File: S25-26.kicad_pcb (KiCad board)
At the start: 6 copper layers, 90 x 90 mm, 139 parts, among them IC1 CMV4000-3E5M0PN, IC10 DS90LV048ATM_NOPB, IC2 MXL86110I-AQB-R, IC3 NCV317BD2TR4G, IC4 MT29F2G01ABAGDWB-IT_G_TR, IC5 MT29F2G01ABAGDWB-IT_G_TR, IC6 XMC7200D-E272K8384AA, IC7 DS90LV011AHMF_NOPB, IC8 DS90LV048ATM_NOPB, IC9 DS90LV048ATM_NOPB, J1 DC_IN_PADS, J2 Conn_01x04_Pin, J3 Conn_01x02_Pin, J4 RJ45_RB1-125B8G1A, Q1 ZXT849K, U1 TPS73601MDRBREP, U2 TPS73601MDRBREP, Y1 DSC1101DM2-012.0000

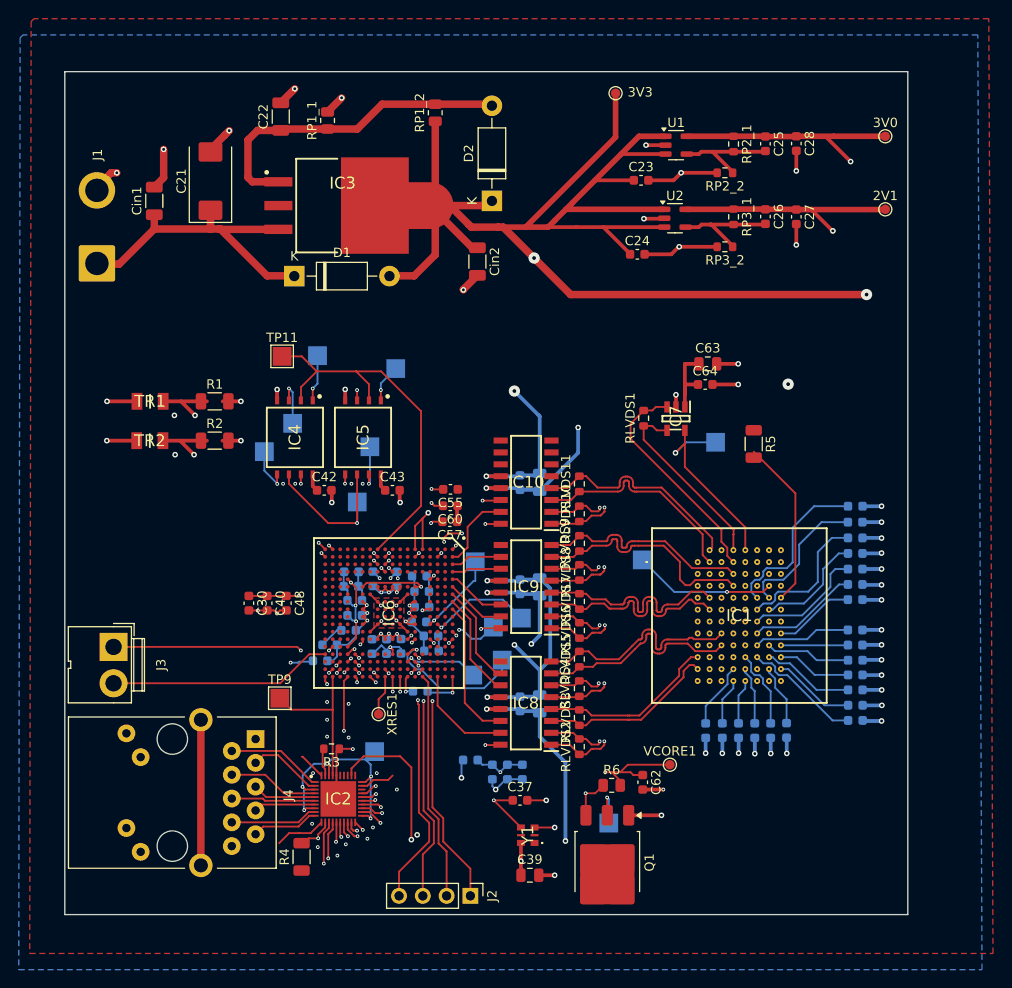
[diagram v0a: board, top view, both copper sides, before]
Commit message: Watch Out: David's Mounting Holes
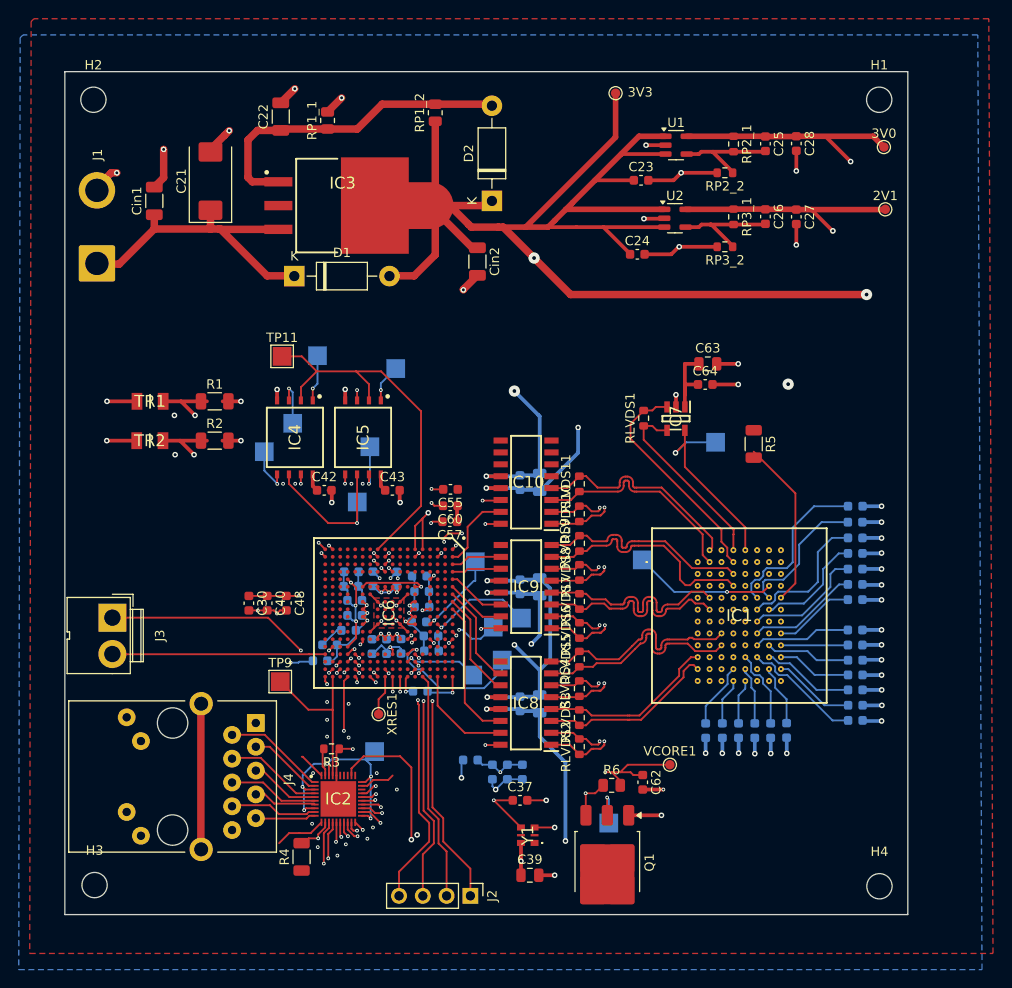
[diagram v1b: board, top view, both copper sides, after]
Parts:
- added H1: MountingHole, MountingHole:MountingHole_2.7mm, F.Cu at (195.3, 53.2)
- added H2: MountingHole, MountingHole:MountingHole_2.7mm, F.Cu at (111.5, 53.2)
- added H3: MountingHole, MountingHole:MountingHole_2.7mm, F.Cu at (111.6, 137.1)
- added H4: MountingHole, MountingHole:MountingHole_2.7mm, F.Cu at (195.4, 137.2)
- moved J3 3.12 mm to (113.5, 108.5)
- moved TP9 1.78 mm to (131.4, 115.3)
- moved J4 1.72 mm to (128.8, 119.7)
- moved 3V0 1.16 mm to (195.8, 58.2)
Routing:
- net /SCB3_RX: track 23.6 -> 25.4 mm
- net /PHY_LED0: track 58.7 -> 60.4 mm
- net /BI_DD_N: track 7.15 -> 5.64 mm
- net /ETH0_REF_CLK: track 16.8 -> 17.6 mm
- net /BI_DB_P: track 9.70 -> 10.5 mm
- net /BI_DA_P: track 10.3 -> 11.0 mm
- net /BI_DB_N: track 6.79 -> 7.54 mm
- net /BI_DC_P: track 8.97 -> 9.72 mm
- net /SCB3_TX: track 23.9 -> 23.2 mm

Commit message: Lots of small changes
Some power and ground planes need to be looked at
All parts need to be reexamined before ordering
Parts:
- removed C21: 10uF, Capacitor_Tantalum_SMD:CP_EIA-7343-31_Kemet-D
- removed C22: 10uF, Capacitor_SMD:C_1206_3216Metric
- removed Cin1, Cin2: 1uF, Capacitor_SMD:C_1206_3216Metric
- removed D2: 1N4002, Diode_THT:D_DO-41_SOD81_P10.16mm_Horizontal
- removed RP1_1: 165, Resistor_SMD:R_0805_2012Metric
- removed RP1_2: 100, Resistor_SMD:R_0805_2012Metric
- added C71: 100uF, Capacitor_SMD:C_1206_3216Metric, F.Cu at (142.9, 64.5)
- added C72: 10nF, Capacitor_SMD:C_1206_3216Metric, F.Cu at (129.0, 71.3)
- added C73: 150pF, Capacitor_SMD:C_1206_3216Metric, F.Cu at (131.4, 59.5)
- added C74: 0.1uF, Capacitor_SMD:C_1206_3216Metric, F.Cu at (135.1, 59.5)
- added C75: 1500pF, Capacitor_SMD:C_1206_3216Metric, F.Cu at (135.2, 64.5)
- added C76: 4.7uF, Capacitor_SMD:C_1206_3216Metric, F.Cu at (116.2, 63.9)
- added C77: 4.7uF, Capacitor_SMD:C_1206_3216Metric, F.Cu at (120.0, 64.0)
- added J5: Conn_01x04_Pin, Connector_PinHeader_2.54mm:PinHeader_1x04_P2.54mm_Vertical, F.Cu at (110.3, 85.4)
- added L1: SRP6060FA-150M, SamacSys_Parts:SRP6060FA150M, F.Cu at (135.2, 70.9)
- added R10: 247k, Resistor_SMD:R_1206_3216Metric, F.Cu at (121.7, 54.0)
- added R11: 33k, Resistor_SMD:R_1206_3216Metric, F.Cu at (127.1, 54.0)
- added R7: 10k, Resistor_SMD:R_1206_3216Metric, F.Cu at (139.1, 64.5)
- added R8: 5.9k, Resistor_SMD:R_1206_3216Metric, F.Cu at (139.0, 59.5)
- added R9: 549, Resistor_SMD:R_1206_3216Metric, F.Cu at (135.1, 54.5)
- D1: value 1N4002 -> MBRS340T3G; footprint Diode_THT:D_DO-41_SOD81_P10.16mm_Horizontal -> SamacSys_Parts:DIOM8059X261N
- IC3: value NCV317BD2TR4G -> TPS5430DDAR; footprint SamacSys_Parts:TO254P1420X457-4N -> SamacSys_Parts:SOIC127P600X170-9N
- J2: value Conn_01x04_Pin -> Conn_01x06_Pin; footprint Connector_PinHeader_2.54mm:PinHeader_1x04_P2.54mm_Vertical -> Connector_PinHeader_2.54mm:PinHeader_1x06_P2.54mm_Vertical
- J3: value Conn_01x02_Pin -> Conn_01x04_Pin; footprint Connector:JWT_A3963_1x02_P3.96mm_Vertical -> Connector_PinHeader_2.54mm:PinHeader_1x04_P2.54mm_Vertical
- J4: value RJ45_RB1-125B8G1A -> RJ45_JXD1-0001NL
- U1, U2: value TPS73601MDRBREP -> TPS73601MDBVREP
- moved J4 17.0 mm to (117.2, 132.2)
- moved IC3 11.2 mm to (126.2, 64.8), turned to 180 degrees
- moved D1 10.9 mm to (122.0, 73.0), turned to 180 degrees
- moved J3 6.18 mm to (110.2, 103.3), turned to 0 degrees
- moved J1 5.28 mm to (111.8, 65.4), turned to -90 degrees
- moved R6 0.28 mm to (166.5, 126.3), turned to 180 degrees
- moved U2 0.13 mm to (173.7, 65.9)
- moved RLVDS1 0.13 mm to (170.3, 87.3)
- moved RLVDS5 0.11 mm to (163.4, 113.0)
- moved RLVDS4 0.10 mm to (163.4, 116.2)
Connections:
- net /JTAG_SWCLK renamed /Processing/SWJ_SWCLK_TCLK
- net /JTAG_SWDIO renamed /Processing/SWJ_SWDIO_TMS
- net /JTAG_SWO renamed /Processing/SWJ_SWO_TDO
- net /JTAG_TDI renamed /Processing/SWJ_SWDOE_TDI
- net /SCB3_RX renamed /Processing/SCB3_RX (P17.1)
- D1 pad 1: /Voltage Regulation/DC_LINE_IN_28V -> Net-(D1-K)
- D1 pad 2: +3V3 -> GND
- IC3 pad 3: /Voltage Regulation/DC_LINE_IN_28V -> unconnected-(IC3-NC_2-Pad3)
- IC3 pad 4: +3V3 -> Net-(IC3-VSENSE)
- IC6 pad A14: unconnected-(IC6B-P2.0-PadA14) -> /Processing/SWJ_TRSTN
- IC6 pad R1: unconnected-(IC6B-P12.0-PadR1) -> /Processing/SCB8_RX
- IC6 pad R2: unconnected-(IC6B-P12.1-PadR2) -> /Processing/SCB8_TX
- IC6 pad R3: unconnected-(IC6B-P12.2-PadR3) -> /Processing/SCB8_RTS
- IC6 pad T1: unconnected-(IC6B-P12.3-PadT1) -> /Processing/SCB8_CTS
- IC6 pad T15: unconnected-(IC6B-P17.4-PadT15) -> /Processing/SCB3_CTS
- IC6 pad U15: unconnected-(IC6B-P17.3-PadU15) -> /Processing/SCB3_RTS
- IC6 pad V15: /SCB3_TX -> /Processing/SCB3_TX (P17.2)
- J3 pad 2: /SCB3_TX -> /Processing/SCB3_CTS
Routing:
- net +3V3: track 543.4 -> 482.0 mm
- net /Processing/SCB8_RX: track 0.00 -> 35.8 mm
- net /Processing/SCB8_TX: track 0.00 -> 33.6 mm, vias 0 -> 2
- net /Processing/SCB8_CTS: track 0.00 -> 33.0 mm
- net /Processing/SCB8_RTS: track 0.00 -> 32.9 mm, vias 0 -> 2
- net GND: track 549.8 -> 517.8 mm, vias 95 -> 90
- net Net-(IC3-BOOT): track 35.1 -> 3.16 mm
- net /Processing/SCB3_CTS: track 0.00 -> 31.8 mm, vias 0 -> 2
- net /Processing/SWJ_TRSTN: track 0.00 -> 31.5 mm, vias 0 -> 2
- net /Processing/SCB3_RTS: track 0.00 -> 28.1 mm, vias 0 -> 2
- net /Processing/SCB3_TX (P17.2): track 0.00 -> 27.7 mm
- net /SCB3_TX: track 23.2 -> 0.00 mm
- net /PHY_LED0: track 60.4 -> 42.1 mm
- net Net-(D1-K): track 0.00 -> 16.9 mm
- net Net-(IC3-ENA): track 0.00 -> 11.5 mm
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- added copper zone on F.Cu, net Net-(IC3-VSENSE)

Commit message: See previous push
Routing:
- net +3V3: track 482.0 -> 486.4 mm
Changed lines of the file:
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@@
+	)
+	(segment
+		(start 159.9 66.9)
+		(end 155.5 66.9)
+		(width 0.8)
+		(layer "F.Cu")
+		(net 2)
 	)
 	(segment

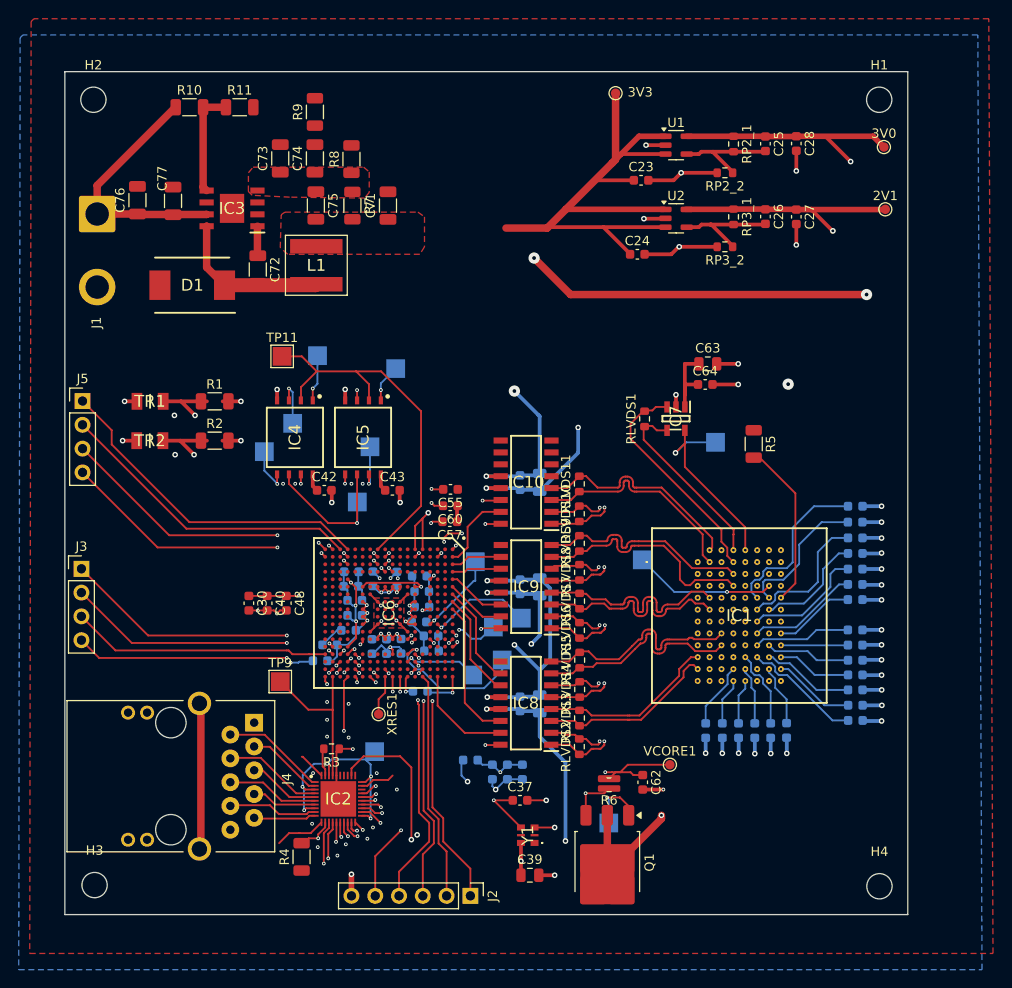
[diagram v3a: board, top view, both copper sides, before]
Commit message: Added text to pinheaders for JTAG and UART
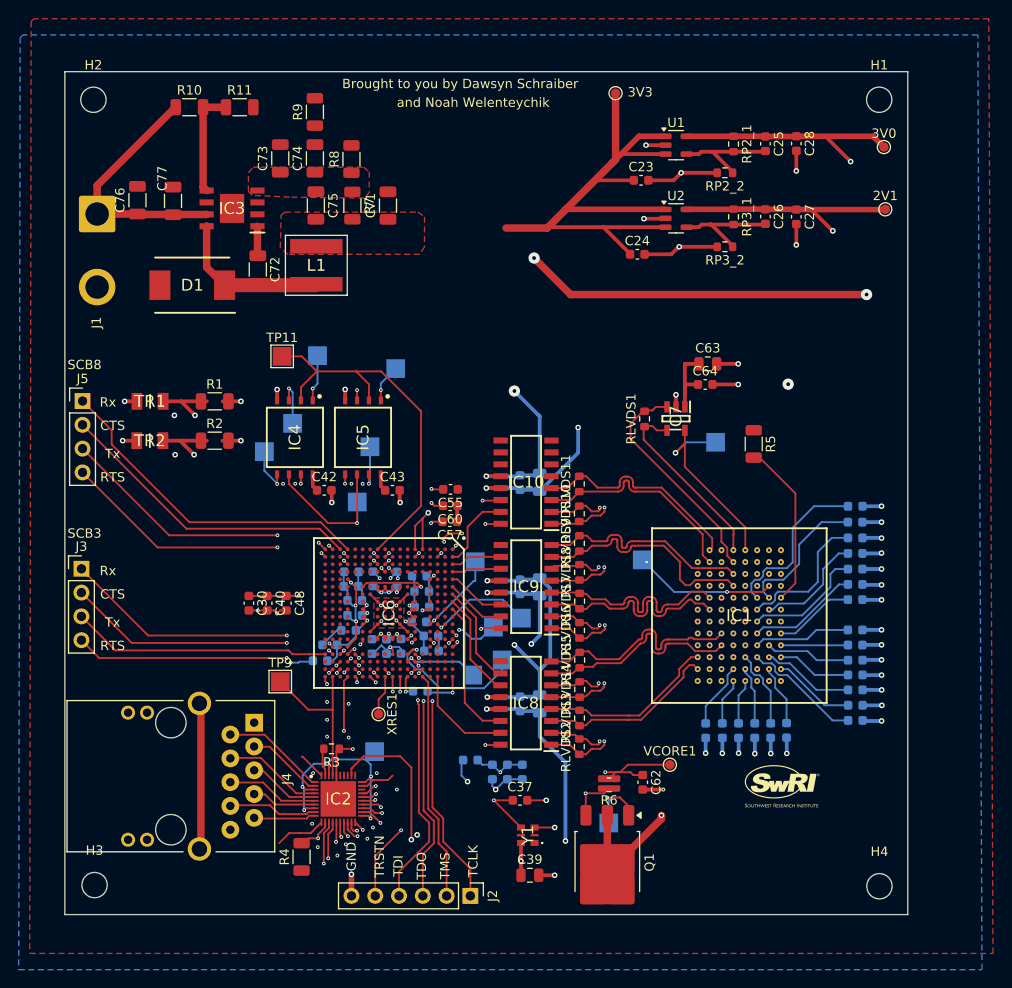
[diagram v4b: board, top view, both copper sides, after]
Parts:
- added G***: LOGO, SamacSys_Parts:swri_Logo, F.Cu at (185.0, 126.5)
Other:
- board text added: "Brought to you by Dawsyn Schraiber"
- board text added: "CTS"
- board text added: "GND"
- board text added: "RTS"
- board text added: "Rx"
- board text added: "SCB3"
- board text added: "SCB8"
- board text added: "TCLK"
- board text added: "TDI"
- board text added: "TDO"
- board text added: "TMS"
- board text added: "TRSTN"
- board text added: "Tx"
- board text added: "and Noah Welenteychik"

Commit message: Almost done
Taking a break and making a push. Known things to do:
Add pull-up resistors to ETH MDIO, ETH MDC, and XRESL.
Source a 100uF capacitor for primary regulator.
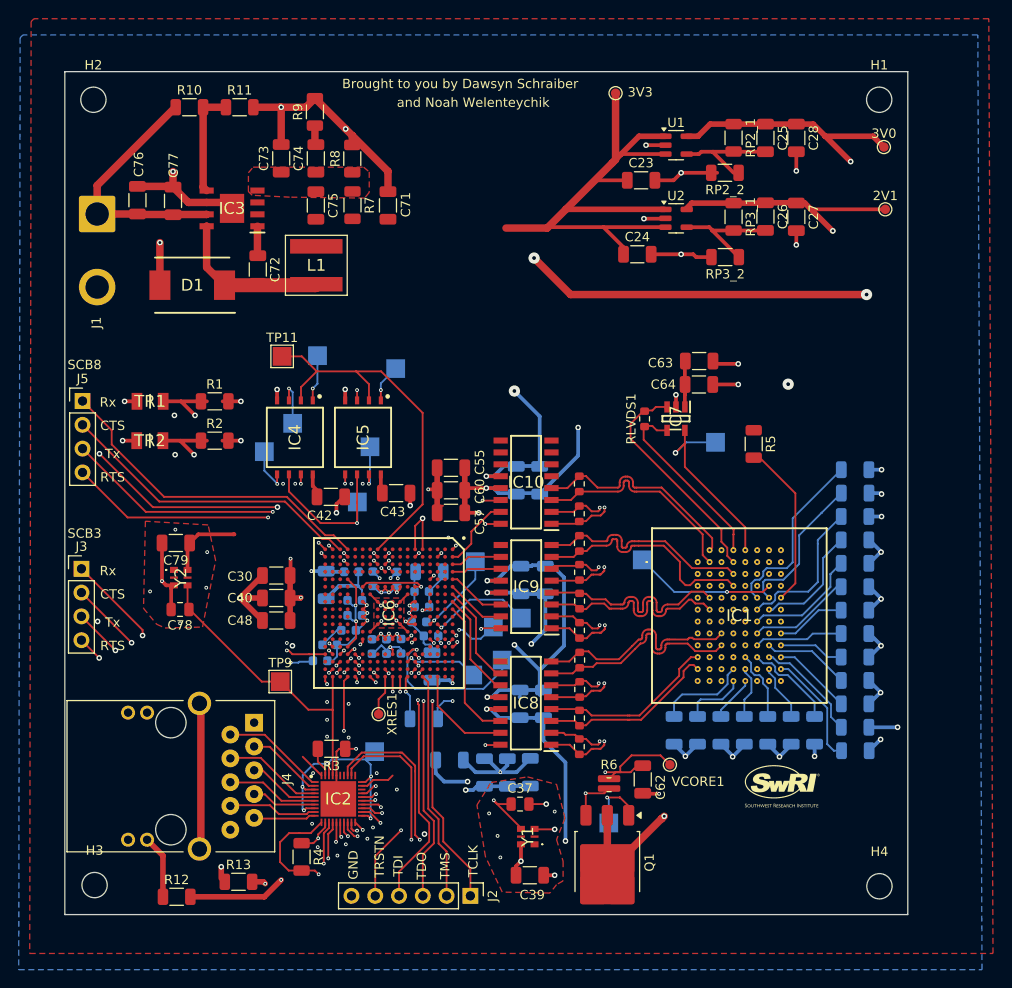
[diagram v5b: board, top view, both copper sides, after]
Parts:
- added C78: 15pF, Capacitor_SMD:C_0805_2012Metric, F.Cu at (120.7, 107.6)
- added C79: 0.1uF, Capacitor_SMD:C_1206_3216Metric, F.Cu at (120.2, 100.5)
- added R12: 60, Resistor_SMD:R_1206_3216Metric, F.Cu at (120.3, 138.3)
- added R13: 56, Resistor_SMD:R_1206_3216Metric, F.Cu at (126.9, 136.7)
- added Y2: DSC1101DM2-125.0000T, SamacSys_Parts:DSC1101DM20120000, F.Cu at (120.8, 104.2)
- C1, C10, C11, C12, C13, C14, C15, C16, C17, C18, C19, C2, C20, C23, C24, C27, C28, C29, C3, C30, C4, C40, C42, C43, C47, C48, C49, C5, C51, C53, C54, C55, C57, C6, C60, C62, C7, C8, C9: footprint Capacitor_SMD:C_0603_1608Metric -> Capacitor_SMD:C_1206_3216Metric
- C25, C26, C52, C58: value 10nF -> 0.01uF; footprint Capacitor_SMD:C_0603_1608Metric -> Capacitor_SMD:C_1206_3216Metric
- C37: footprint Capacitor_SMD:C_0603_1608Metric -> Capacitor_SMD:C_0805_2012Metric
- C39, C63, C68, C69, C70: footprint Capacitor_SMD:C_0805_2012Metric -> Capacitor_SMD:C_1206_3216Metric
- C64: value 1nF -> 0.01uF; footprint Capacitor_SMD:C_0603_1608Metric -> Capacitor_SMD:C_1206_3216Metric
- C65, C66, C67: value 1nF -> 1000pF; footprint Capacitor_SMD:C_0603_1608Metric -> Capacitor_SMD:C_1206_3216Metric
- C72: value 10nF -> 0.01uF
- R10: value 247k -> 249k
- R3, RP2_1, RP2_2, RP3_1, RP3_2: footprint Resistor_SMD:R_0603_1608Metric -> Resistor_SMD:R_1206_3216Metric
- moved C18 4.85 mm to (192.8, 122.7)
- moved C1 4.48 mm to (188.4, 120.5), turned to 90 degrees
- moved C30 4.15 mm to (131.0, 104.0), turned to 180 degrees
- moved C13 3.99 mm to (192.8, 120.2)
- moved C5 3.90 mm to (192.8, 92.7)
- moved C19 3.37 mm to (173.4, 120.5), turned to 90 degrees
- moved C10 3.10 mm to (192.8, 95.2)
- moved C17 3.09 mm to (192.8, 117.7)
- moved C49 2.97 mm to (146.7, 119.3)
- moved C29 2.65 mm to (136.3, 105.0), turned to 90 degrees
- moved C20 2.65 mm to (175.9, 120.5), turned to 90 degrees
- moved C55 2.30 mm to (149.6, 92.5)
- moved C6 2.28 mm to (192.8, 97.7)
- moved C51 2.22 mm to (149.5, 123.7)
- moved C12 2.16 mm to (192.8, 115.2)
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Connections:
- C19 pad 1: Net-(IC1-VREF) -> GND
- C19 pad 2: GND -> Net-(IC1-VREF)
- C20 pad 1: Net-(IC1-REF_ADC) -> GND
- C20 pad 2: GND -> Net-(IC1-REF_ADC)
- IC2 pad 32: /PHY_LED0 -> Net-(IC2-GPHY_LED0/CFG_EXT)
- IC2 pad 33: /PHY_LED1 -> Net-(IC2-GPHY_LED1/CFG_LDO0)
- J4 pad L3: /PHY_LED0 -> /PHY_LED1
- R4 pad 1: +3V3 -> /HRSTN
- R4 pad 2: /HRSTN -> +3V3
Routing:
- net +3V3: track 486.4 -> 541.1 mm, vias 29 -> 32
- net Net-(IC2-GPHY_LED0/CFG_EXT): track 0.00 -> 42.0 mm, vias 0 -> 2
- net Net-(IC2-GPHY_LED1/CFG_LDO0): track 0.00 -> 37.4 mm, vias 0 -> 2
- net /PHY_LED0: track 42.1 -> 6.79 mm, vias 1 -> 0
- net /PHY_LED1: track 0.00 -> 21.5 mm, vias 0 -> 1
- net /ETH0_REF_CLK: track 17.6 -> 33.2 mm
- net GND: track 517.8 -> 531.0 mm, vias 90 -> 99
- net /Processing/EXT_PS_CTL1: track 70.1 -> 80.4 mm
- net Net-(IC1-LVDS): track 8.77 -> 12.3 mm
- net Net-(IC1-VREF): track 7.02 -> 9.88 mm
- net Net-(IC1-RAMP): track 12.8 -> 9.96 mm
- net Net-(C74-Pad2): track 0.00 -> 2.07 mm
- net Net-(IC1-REF_ADC): track 5.01 -> 6.74 mm
- net Net-(IC1-ADC): track 9.88 -> 11.6 mm
- net Net-(IC1-CMD_P__INV): track 18.0 -> 19.4 mm
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
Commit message: See previous push
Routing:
- net +3V3: track 541.1 -> 540.6 mm
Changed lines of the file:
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@@
+	)
+	(segment
+		(start 141.8 110.55)
+		(end 142.15 110.2)
+		(width 0.2)
+		(layer "F.Cu")
+		(net 2)
 	)
 	(segment
@@
 		(end 159.9 66.9)
 		(width 0.8)
-		(layer "F.Cu")
-		(net 2)
-	)
-	(segment
-		(start 141.8 110.55)
-		(end 142.15 110.2)
-		(width 0.2)
 		(layer "F.Cu")
 		(net 2)
@@
 		(end 133.45 131.5)
 		(width 0.2)
+		(layer "F.Cu")
+		(net 2)
+	)
+	(segment
+		(start 159.9 66.9)
+		(end 156 66.9)
+		(width 0.8)
 		(layer "F.Cu")
 		(net 2)
@@
 		(layer "F.Cu")
 		(net 2)
-	)
-	(segment
-		(start 159.9 66.9)
-		(end 155.5 66.9)
-		(width 0.8)
-		(layer "F.Cu")
-		(net 2)
